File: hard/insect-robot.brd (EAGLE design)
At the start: 100 x 80 mm, 13 parts, among them Q1 AO3400, SW1 MK-12C02, U1 ATMEGA328P-QFN32, U2 PW0316

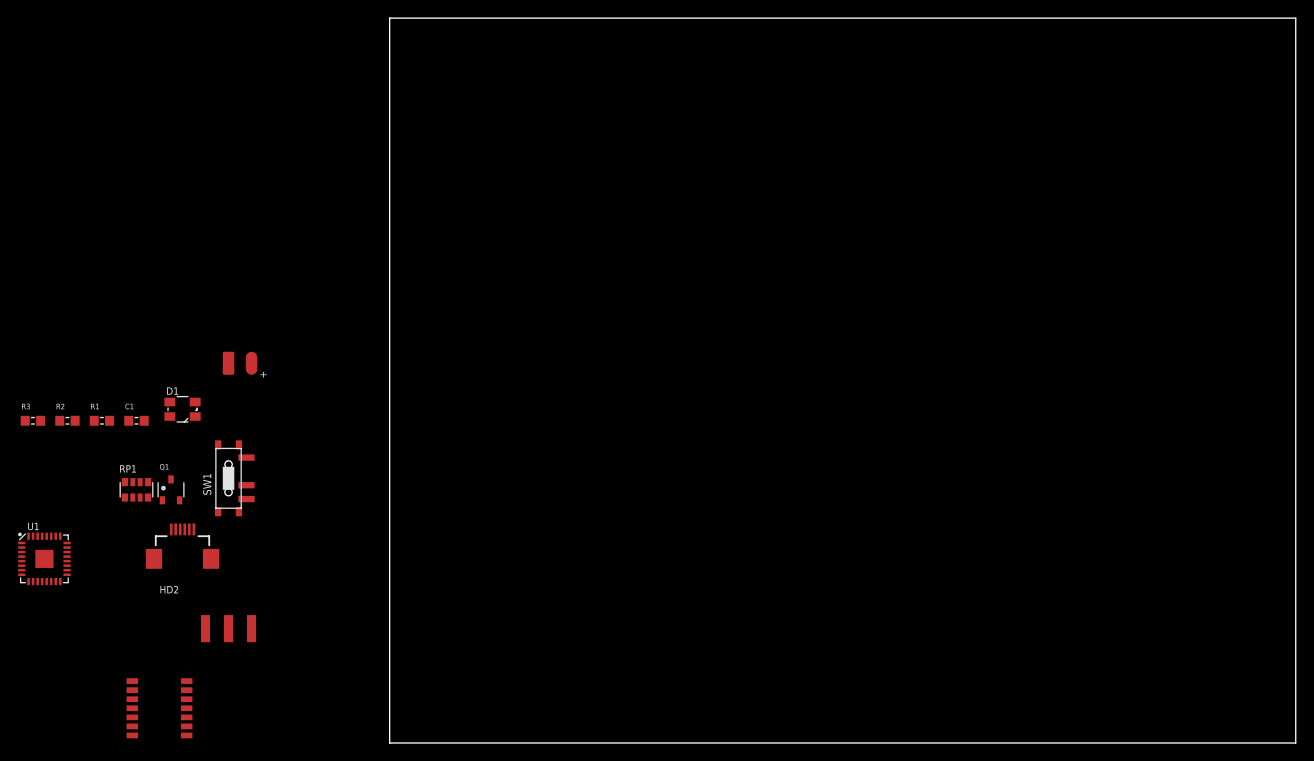
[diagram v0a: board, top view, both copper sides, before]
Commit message: Place the components
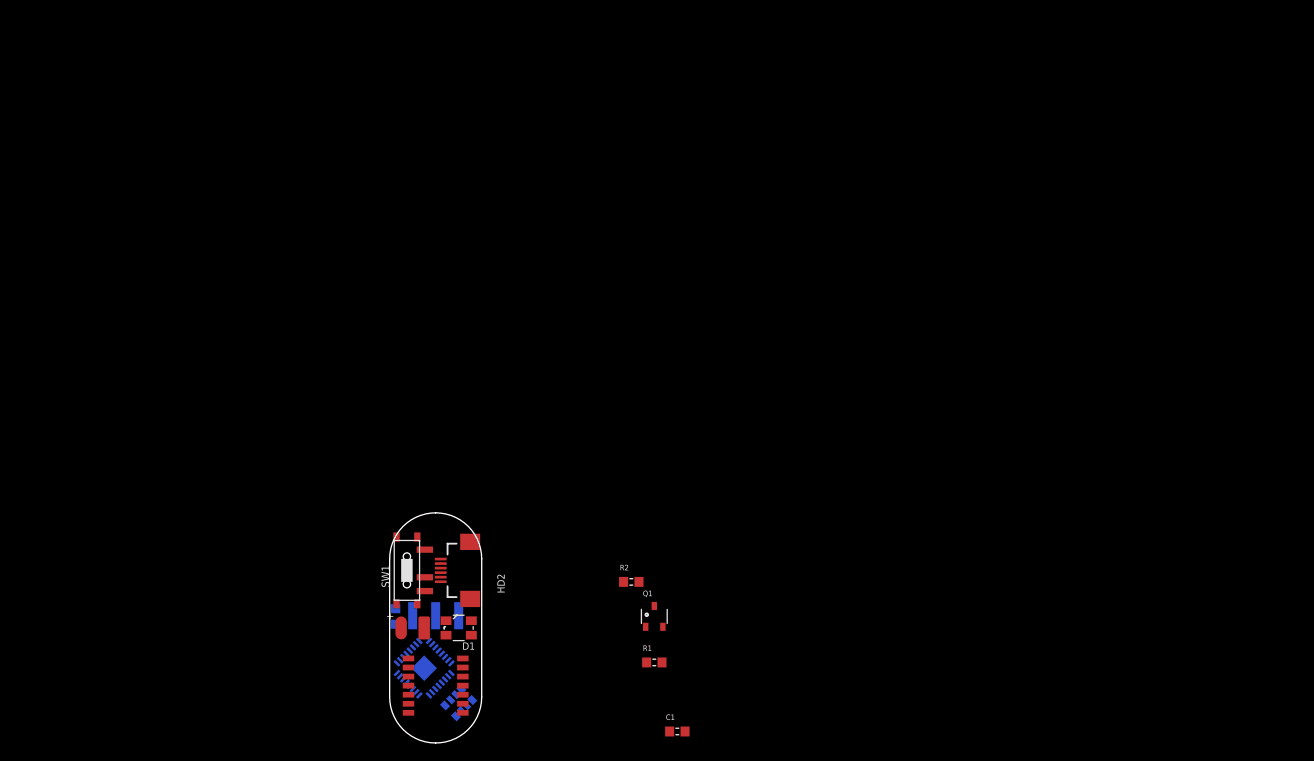
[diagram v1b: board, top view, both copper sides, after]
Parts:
- moved C1 68.8 mm to (31.8, 1.27)
- moved R1 66.5 mm to (29.2, 8.89)
- moved R2 64.7 mm to (26.7, 17.8)
- moved Q1 55.1 mm to (29.2, 14.0)
- moved R3 45.5 mm to (0.64, 14.0), flipped to the bottom, turned to 270 degrees
- moved U1 43.6 mm to (3.81, 8.26), flipped to the bottom, turned to 315 degrees
- moved RP1 42.6 mm to (7.62, 4.45), flipped to the bottom, turned to 315 degrees
- moved D1 38.9 mm to (7.62, 12.7), turned to 180 degrees
- moved BAT1 34.9 mm to (2.54, 12.7), turned to 180 degrees
- moved HD2 31.8 mm to (8.89, 19.1), turned to 90 degrees
- moved U2 30.5 mm to (5.08, 5.08), turned to 180 degrees
- moved HD1 25.6 mm to (8.89, 19.1), flipped to the bottom, turned to 180 degrees
- moved SW1 22.2 mm to (1.91, 19.1)
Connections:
- net N$1 renamed RR-
- net N$2 renamed RG-
- net N$3 renamed RB-
- net N$4 renamed R-
- net N$5 renamed G-
- net N$6 renamed B-
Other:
- board size 100 x 80 mm -> 10.2 x 25.4 mm

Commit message: Place components
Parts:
- moved R2 28.4 mm to (0.64, 6.35), flipped to the bottom, turned to 270 degrees
- moved R1 27.3 mm to (2.54, 3.17), flipped to the bottom, turned to 225 degrees
- moved Q1 26.9 mm to (2.54, 10.8), flipped to the bottom, turned to 45 degrees
- moved C1 24.2 mm to (7.62, 2.54), flipped to the bottom, turned to 135 degrees
- moved RP1 5.71 mm to (7.62, 10.2), turned to 45 degrees
- moved U1 2.29 mm to (5.08, 6.35), turned to 225 degrees
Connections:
- net N$7 renamed AREF

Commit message: Redraw some components
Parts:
- HD2: value HEADER1X6-FPC0.5 -> HEADER1X6-SS-FPC0.5-DRAWER; device MyLibrary:FPC0.5-6 -> MyLibrary:FPC0.5-6-DRAWER
- SW1: value MK-12C02 -> SWITCH-DT; device Seeed-OPL-Button:SW7-SMD-L6.7X2.7X3.2MM -> MyLibrary:SWITCH-SMD-6.7X2.7
- moved R2 3.42 mm to (1.91, 3.17), turned to 225 degrees
- moved R1 3.17 mm to (5.08, 1.27), turned to 180 degrees
- moved C1 0.90 mm to (8.26, 3.17)
- moved HD2 0.63 mm to (9.53, 19.1)
- moved Q1 0.32 mm to (2.54, 10.5)
- moved R3 0.32 mm to (0.95, 14.0)
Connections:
- net GND: now also HD2.SS1, HD2.SS2, SW1.SS1, SW1.SS2, SW1.SS3, SW1.SS4

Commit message: Route some wires
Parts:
- BAT1: value BATTERY-SMD -> BATTERY-SMD-SMALL; device MyLibrary:BAT-SMD -> MyLibrary:BAT-SMD-SMALL
- moved D1 2.54 mm to (5.08, 12.7), turned to 270 degrees
- moved BAT1 0.64 mm to (1.91, 12.7), turned to 0 degrees
- moved Q1 0.63 mm to (2.54, 9.84)
- moved U1 0.63 mm to (5.08, 5.71)
- moved R2 0.32 mm to (1.91, 2.86)
- moved C1 0.22 mm to (8.10, 3.33), turned to 315 degrees
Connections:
- net B-: now also RP1.1; no longer RP1.5
- net R-: now also RP1.5; no longer RP1.1
- net RB-: now also RP1.2; no longer RP1.6
- net RR-: now also RP1.6; no longer RP1.2
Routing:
- net LINK: track 0.00 -> 22.1 mm, vias 0 -> 1
- net R: track 0.00 -> 19.3 mm, vias 0 -> 2
- net VBAT: track 0.00 -> 10.6 mm, vias 0 -> 2
- net R-TX: track 0.00 -> 10.4 mm, vias 0 -> 1
- net SWITCH-B: track 0.00 -> 8.39 mm, vias 0 -> 1
- net BAT-COM: track 0.00 -> 5.73 mm
- net RR-: track 0.00 -> 5.66 mm, vias 0 -> 2
- net R-BCTS: track 0.00 -> 5.64 mm, vias 0 -> 1
- net RXD: track 0.00 -> 4.27 mm
- net TXD: track 0.00 -> 3.78 mm, vias 0 -> 1
- net BRTS: track 0.00 -> 3.43 mm, vias 0 -> 1
- net RG-: track 0.00 -> 2.61 mm
- net L: track 0.00 -> 2.35 mm
- net RB-: track 0.00 -> 2.21 mm
- net BCTS: track 0.00 -> 2.05 mm
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
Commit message: Done routing
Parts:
- moved RP1 3.82 mm to (4.76, 12.7), flipped to the top, turned to 270 degrees
- moved D1 2.86 mm to (7.94, 12.7)
- moved R3 2.22 mm to (0.95, 16.2), turned to 90 degrees
- moved Q1 0.90 mm to (3.17, 10.5)
- moved R2 0.57 mm to (2.38, 3.17)
- moved BAT1 0.32 mm to (1.59, 12.7)
- moved R1 0.22 mm to (5.24, 1.11)
- turned C1 to 135 degrees
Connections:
- removed net RST: HD2.5, U1.29
- net B-: now also RP1.3; no longer RP1.1
- net G-: now also RP1.5; no longer RP1.3
- net R-: now also RP1.7; no longer RP1.5
- net RB-: now also RP1.4; no longer RP1.2
- net RG-: now also RP1.6; no longer RP1.4
- net RR-: now also RP1.8; no longer RP1.6
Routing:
- net VBAT: track 10.6 -> 38.2 mm, vias 2 -> 3
- net MOSI: track 0.00 -> 18.2 mm, vias 0 -> 1
- net MISO: track 0.00 -> 17.5 mm, vias 0 -> 1
- net SCK: track 0.00 -> 17.5 mm, vias 0 -> 1
- net L: track 2.35 -> 17.3 mm, vias 0 -> 2
- net RG-: track 2.61 -> 10.1 mm, vias 0 -> 1
- net RB-: track 2.21 -> 9.52 mm, vias 0 -> 1
- net GND: track 0.04 -> 5.42 mm, vias 0 -> 7
- net BAT-COM: track 5.73 -> 9.38 mm, vias 0 -> 2
- net G-: track 0.00 -> 3.54 mm
- net B-: track 0.00 -> 3.54 mm
- net R: track 19.3 -> 16.5 mm
- net SWITCH-B: track 8.39 -> 5.71 mm
- net R-BCTS: track 5.64 -> 3.51 mm
- net R-: track 0.00 -> 1.81 mm
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- added copper zone on layer 1, net GND
- added copper zone on layer 16, net GND
